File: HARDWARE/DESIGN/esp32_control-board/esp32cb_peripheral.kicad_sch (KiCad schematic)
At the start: 7 parts, among them J309 Lamp1

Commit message: 60825 - Schematic update and PCB-layout started
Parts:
- removed D318, D319: LOCK on, LED_SMD:LED_0603_1608Metric, symbol Device:LED
- removed R334, R335: 5k1, Resistor_SMD:R_0603_1608Metric, symbol Device:R
- added C202: 1u, Capacitor_SMD:C_0603_1608Metric, symbol Device:C
- added C211: 100n, Capacitor_SMD:C_0603_1608Metric, symbol Device:C
- added C212, C213, C214, C215, C220, C221: 10n, Capacitor_SMD:C_0603_1608Metric, symbol Device:C
- added C218, C219: 4u7, Capacitor_SMD:C_0805_2012Metric, symbol Device:C
- added D112, D113, D114, D115: XL-1608UWC-04, LED_SMD:LED_0603_1608Metric, symbol Device:LED
- added J201: RFID-module1, Connector_JST:JST_PH_B8B-PH-K_1x08_P2.00mm_Vertical, symbol Connector:Screw_Terminal_01x08
- added J402, J403: B4B-PH-K-S(LF)(SN), Connector_JST:JST_PH_B4B-PH-K_1x04_P2.00mm_Vertical, symbol Connector_Generic:Conn_01x04
- added J404: B2B-PH-K-S(LF)(SN), symbol Connector_Generic:Conn_01x02
- added J405, J406, J407, J408, J411, J412: B3B-PH-K-S(LF)(SN), Connector_JST:JST_PH_B3B-PH-K_1x03_P2.00mm_Vertical, symbol Connector_Generic:Conn_01x03
- added R125, R127, R129, R130: 12k, Resistor_SMD:R_0603_1608Metric, symbol Device:R
- added R126, R128, R131, R132: 120, Resistor_SMD:R_0603_1608Metric, symbol Device:R
- added R422, R423, R424, R425, R426, R427: 1k, Resistor_SMD:R_0603_1608Metric, symbol Device:R
- added U205: USBLC6-2SC6, Package_TO_SOT_SMD:SOT-23-6, symbol Power_Protection:USBLC6-2SC6
- added U401: SN74LVC125ADR, footprint:SOIC-14_L8.7-W3.9-P1.27-LS6.0-BL, symbol (LOGIC):SN74LVC125ADR
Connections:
- net GND: now also C202.2, C211.1, C212.2, C213.2, C214.2, C215.2, C218.1, C219.1, C220.2, C221.2, J201.6 (Pin_6), J402.2 (Pin_2), J403.2 (Pin_2), J405.2 (Pin_2), J406.2 (Pin_2), J407.2 (Pin_2), J408.2 (Pin_2), J411.2 (Pin_2), J412.2 (Pin_2), R125.2, R127.2, R129.2, R130.2, R424.1, R425.1, R426.1, R427.1, U205.2 (GND), U401.1 (1OE#), U401.10 (3OE#), U401.13 (4OE#), U401.4 (2OE#), U401.7 (GND)
- new net: D115.1 (K), R427.2
- new net: D112.1 (K), R424.2
- new net: D114.1 (K), R426.2
- new net: D113.1 (K), R425.2
- new net +3V3: C202.1, C211.2, C218.2, C219.2, J201.8 (Pin_8), J402.1 (Pin_1), J403.1 (Pin_1), J405.1 (Pin_1), J406.1 (Pin_1), J407.1 (Pin_1), J408.1 (Pin_1), J411.1 (Pin_1), J412.1 (Pin_1), U401.14 (VCC)
- new net I2C_scl: J402.4 (Pin_4)
- new net I2C_sda: J402.3 (Pin_3)
- new net RFID1_irq: J201.5 (Pin_5)
- new net RFID1_reset: J201.7 (Pin_7)
- new net SPI_cs1: J201.1 (Pin_1)
- new net SPI_miso: J201.4 (Pin_4)
- new net SPI_mosi: J201.3 (Pin_3)
- new net SPI_sck: J201.2 (Pin_2)
- new net Vusb: U205.5 (VBUS)
- new net di_SENSOR_buf-in1: C212.1, R126.2, U401.2 (1A)
- new net di_SENSOR_buf-in2: C213.1, R128.2, U401.5 (2A)
- new net di_SENSOR_buf-in3: C214.1, R131.2, U401.9 (3A)
- new net di_SENSOR_buf-in4: C215.1, R132.2, U401.12 (4A)
- new net di_SENSOR_buf-out1: D112.2 (A), U401.3 (1Y)
- new net di_SENSOR_buf-out2: D113.2 (A), U401.6 (2Y)
- new net di_SENSOR_buf-out3: D114.2 (A), U401.8 (3Y)
- new net di_SENSOR_buf-out4: D115.2 (A), U401.11 (4Y)
- new net di_SENSOR_ext1: J405.3 (Pin_3), R125.1, R126.1
- new net di_SENSOR_ext2: J406.3 (Pin_3), R127.1, R128.1
- new net di_SENSOR_ext3: J407.3 (Pin_3), R129.1, R131.1
- new net di_SENSOR_ext4: J408.3 (Pin_3), R130.1, R132.1
- new net esp_ADC1-5_esd: R422.1, U205.6 (I/O1)
- new net esp_ADC1-5_in: J411.3 (Pin_3), U205.1 (I/O1)
- new net esp_ADC1-6_esd: R423.1, U205.4 (I/O2)
- new net esp_ADC1-6_in: J412.3 (Pin_3), U205.3 (I/O2)
- new net esp_ADC1_ch5: C220.1, R422.2
- new net esp_ADC1_ch6: C221.1, R423.2
- new net esp_RXD: J403.4 (Pin_4)
- new net esp_TXD: J403.3 (Pin_3)
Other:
- note added: "Analog Inputs"
- note added: "Digital Inputs"
- note added: "Interfaces"
- note added: "RFID-module connector"
- moved on the sheet: D317, J309, R333

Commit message: 60828 - Schematic updated, preliminary PCB-layout done
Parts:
- D317, J309, R333: now not fitted; now left out of the parts list
- J402: value B4B-PH-K-S(LF)(SN) -> I2C
- J403: value B4B-PH-K-S(LF)(SN) -> UART
- J405: value B3B-PH-K-S(LF)(SN) -> Din1; footprint Connector_JST:JST_PH_B3B-PH-K_1x03_P2.00mm_Vertical -> Connector_JST:JST_PH_S3B-PH-K_1x03_P2.00mm_Horizontal; LCSC C131339 -> (none)
- J406: value B3B-PH-K-S(LF)(SN) -> Din3
- J407: value B3B-PH-K-S(LF)(SN) -> Din2; footprint Connector_JST:JST_PH_B3B-PH-K_1x03_P2.00mm_Vertical -> Connector_JST:JST_PH_S3B-PH-K_1x03_P2.00mm_Horizontal; LCSC C131339 -> (none)
- J408: value B3B-PH-K-S(LF)(SN) -> Din4
- J411: value B3B-PH-K-S(LF)(SN) -> Ain2
- J412: value B3B-PH-K-S(LF)(SN) -> Ain1; footprint Connector_JST:JST_PH_B3B-PH-K_1x03_P2.00mm_Vertical -> Connector_JST:JST_PH_S3B-PH-K_1x03_P2.00mm_Horizontal; LCSC C131339 -> (none)
- U401: footprint footprint:SOIC-14_L8.7-W3.9-P1.27-LS6.0-BL -> Package_SO:SOIC-14_3.9x8.7mm_P1.27mm
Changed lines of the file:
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@@
 	(title_block
 		(title "ESP32-based Control Board")
-		(date "2026-08-25")
+		(date "2026-08-28")
 		(rev "2a")
 	)
@@
 			)
 		)
-		(property "Value" "B3B-PH-K-S(LF)(SN)"
+		(property "Value" "Ain2"
 			(at 59.69 226.06 0)
 			(show_name no)
@@
 			)
 		)
-		(property "Value" "B4B-PH-K-S(LF)(SN)"
+		(property "Value" "I2C"
 			(at 77.216 363.22 0)
 			(show_name no)
@@
 			)
 		)
-		(property "Value" "B3B-PH-K-S(LF)(SN)"
+		(property "Value" "Din2"
 			(at 86.36 120.65 0)
 			(show_name no)
@@
 			)
 		)
-		(property "Footprint" "Connector_JST:JST_PH_B3B-PH-K_1x03_P2.00mm_Vertical"
+		(property "Footprint" "Connector_JST:JST_PH_S3B-PH-K_1x03_P2.00mm_Horizontal"
 			(at 88.9 121.92 0)
 			(hide yes)
@@
 			)
 		)
-		(property "LCSC" "C131339"
+		(property "LCSC" ""
 			(at 88.9 121.92 0)
 			(hide yes)
@@
 			)
 		)
-		(property "Value" "B4B-PH-K-S(LF)(SN)"
+		(property "Value" "UART"
 			(at 204.216 363.22 0)
 			(show_name no)
@@
 			)
 		)
-		(property "Value" "B3B-PH-K-S(LF)(SN)"
+		(property "Value" "Din1"
 			(at 86.36 45.72 0)
 			(show_name no)
@@
 			)
 		)
-		(property "Footprint" "Connector_JST:JST_PH_B3B-PH-K_1x03_P2.00mm_Vertical"
+		(property "Footprint" "Connector_JST:JST_PH_S3B-PH-K_1x03_P2.00mm_Horizontal"
 			(at 88.9 46.99 0)
 			(hide yes)
@@
 			)
 		)
-		(property "LCSC" "C131339"
+		(property "LCSC" ""
 			(at 88.9 46.99 0)
 			(hide yes)
@@
 			)
 		)
-		(property "Value" "B3B-PH-K-S(LF)(SN)"
+		(property "Value" "Din3"
 			(at 86.36 82.55 0)
 			(show_name no)
@@
 			)
 		)
-		(property "Footprint" "footprint:SOIC-14_L8.7-W3.9-P1.27-LS6.0-BL"
+		(property "Footprint" "Package_SO:SOIC-14_3.9x8.7mm_P1.27mm"
 			(at 360.68 113.03 0)
 			(hide yes)
@@
 			)
 		)
+		(property "Property" ""
+			(at 360.68 102.87 0)
+			(show_name no)
+			(do_not_autoplace no)
+			(effects
+				(font
+					(size 1.27 1.27)
+				)
+			)
+		)
 		(pin "9"
 		)
@@
 		(body_style 1)
 		(exclude_from_sim no)
-		(in_bom yes)
-		(on_board yes)
-		(in_pos_files yes)
-		(dnp no)
+		(in_bom no)
+		(on_board no)
+		(in_pos_files no)
+		(dnp yes)
 		(property "Reference" "J309"
 			(at 429.26 373.38 0)
@@
 			)
 		)
-		(property "Value" "B3B-PH-K-S(LF)(SN)"
+		(property "Value" "Ain1"
 			(at 59.69 279.4 0)
 			(show_name no)
@@
 			)
 		)
-		(property "Footprint" "Connector_JST:JST_PH_B3B-PH-K_1x03_P2.00mm_Vertical"
+		(property "Footprint" "Connector_JST:JST_PH_S3B-PH-K_1x03_P2.00mm_Horizontal"
 			(at 62.23 280.67 0)
 			(hide yes)
@@
 			)
 		)
-		(property "LCSC" "C131339"
+		(property "LCSC" ""
 			(at 62.23 280.67 0)
 			(hide yes)
@@
 			)
 		)
-		(property "Value" "B3B-PH-K-S(LF)(SN)"
+		(property "Value" "Din4"
 			(at 86.36 157.48 0)
 			(show_name no)
@@
 		(body_style 1)
 		(exclude_from_sim no)
-		(in_bom yes)
-		(on_board yes)
-		(in_pos_files yes)
-		(dnp no)
+		(in_bom no)
+		(on_board no)
+		(in_pos_files no)
+		(dnp yes)
 		(property "Reference" "R333"
 			(at 420.37 362.712 90)
@@
 		(body_style 1)
 		(exclude_from_sim no)
-		(in_bom yes)
-		(on_board yes)
-		(in_pos_files yes)
-		(dnp no)
+		(in_bom no)
+		(on_board no)
+		(in_pos_files no)
+		(dnp yes)
 		(property "Reference" "D317"
 			(at 439.42 359.156 0)

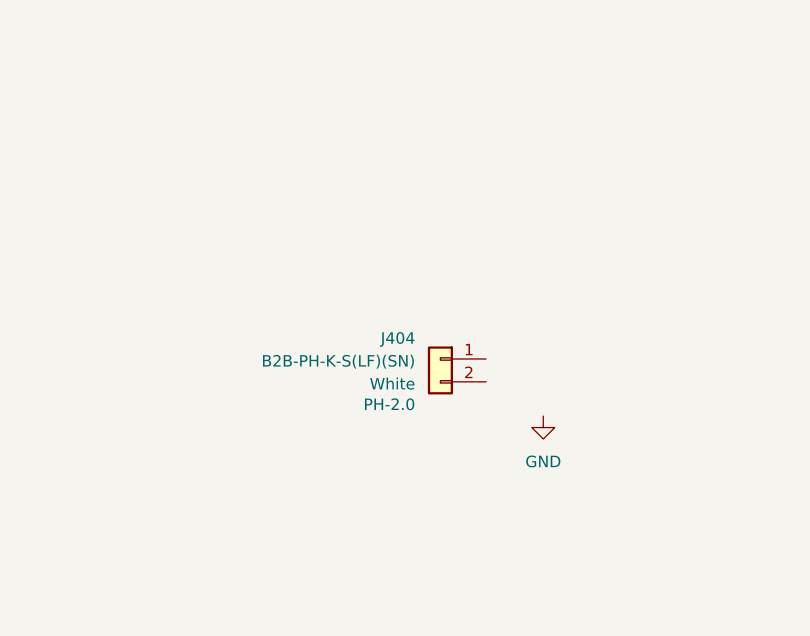
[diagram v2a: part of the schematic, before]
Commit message: 60905 - fuse-holder replaced, led-strip connector added
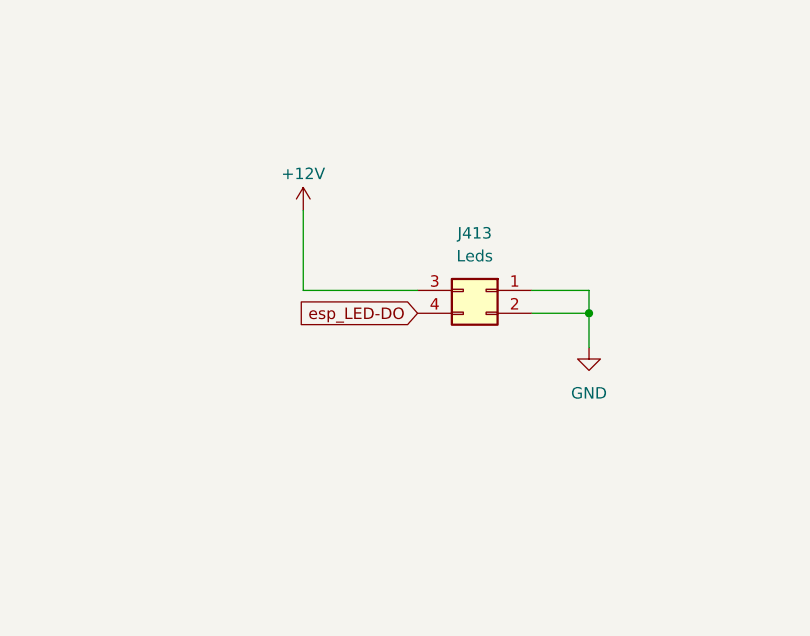
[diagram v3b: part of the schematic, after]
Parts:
- removed J404: B2B-PH-K-S(LF)(SN), symbol Connector_Generic:Conn_01x02
- added J413: Leds, Connector_Molex:Molex_Micro-Fit_3.0_43045-0400_2x02_P3.00mm_Horizontal, symbol Connector_Generic:Conn_02x02_Top_Bottom
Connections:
- net GND: now also J413.1 (Pin_1), J413.2 (Pin_2)
- new net +12V: J413.3 (Pin_3)
- new net esp_LED-DO: J413.4 (Pin_4)

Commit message: 60908 - PCB-layout updated
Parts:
- J201: value RFID-module1 -> RFID-module; footprint Connector_JST:JST_PH_B8B-PH-K_1x08_P2.00mm_Vertical -> Connector_JST:JST_PH_S8B-PH-K_1x08_P2.00mm_Horizontal
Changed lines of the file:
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@@
 			)
 		)
-		(property "Value" "RFID-module1"
+		(property "Value" "RFID-module"
 			(at 377.19 254.254 0)
 			(show_name no)
@@
 			)
 		)
-		(property "Footprint" "Connector_JST:JST_PH_B8B-PH-K_1x08_P2.00mm_Vertical"
+		(property "Footprint" "Connector_JST:JST_PH_S8B-PH-K_1x08_P2.00mm_Horizontal"
 			(at 374.65 254 0)
 			(hide yes)
